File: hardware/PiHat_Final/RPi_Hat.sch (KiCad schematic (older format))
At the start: 0 parts

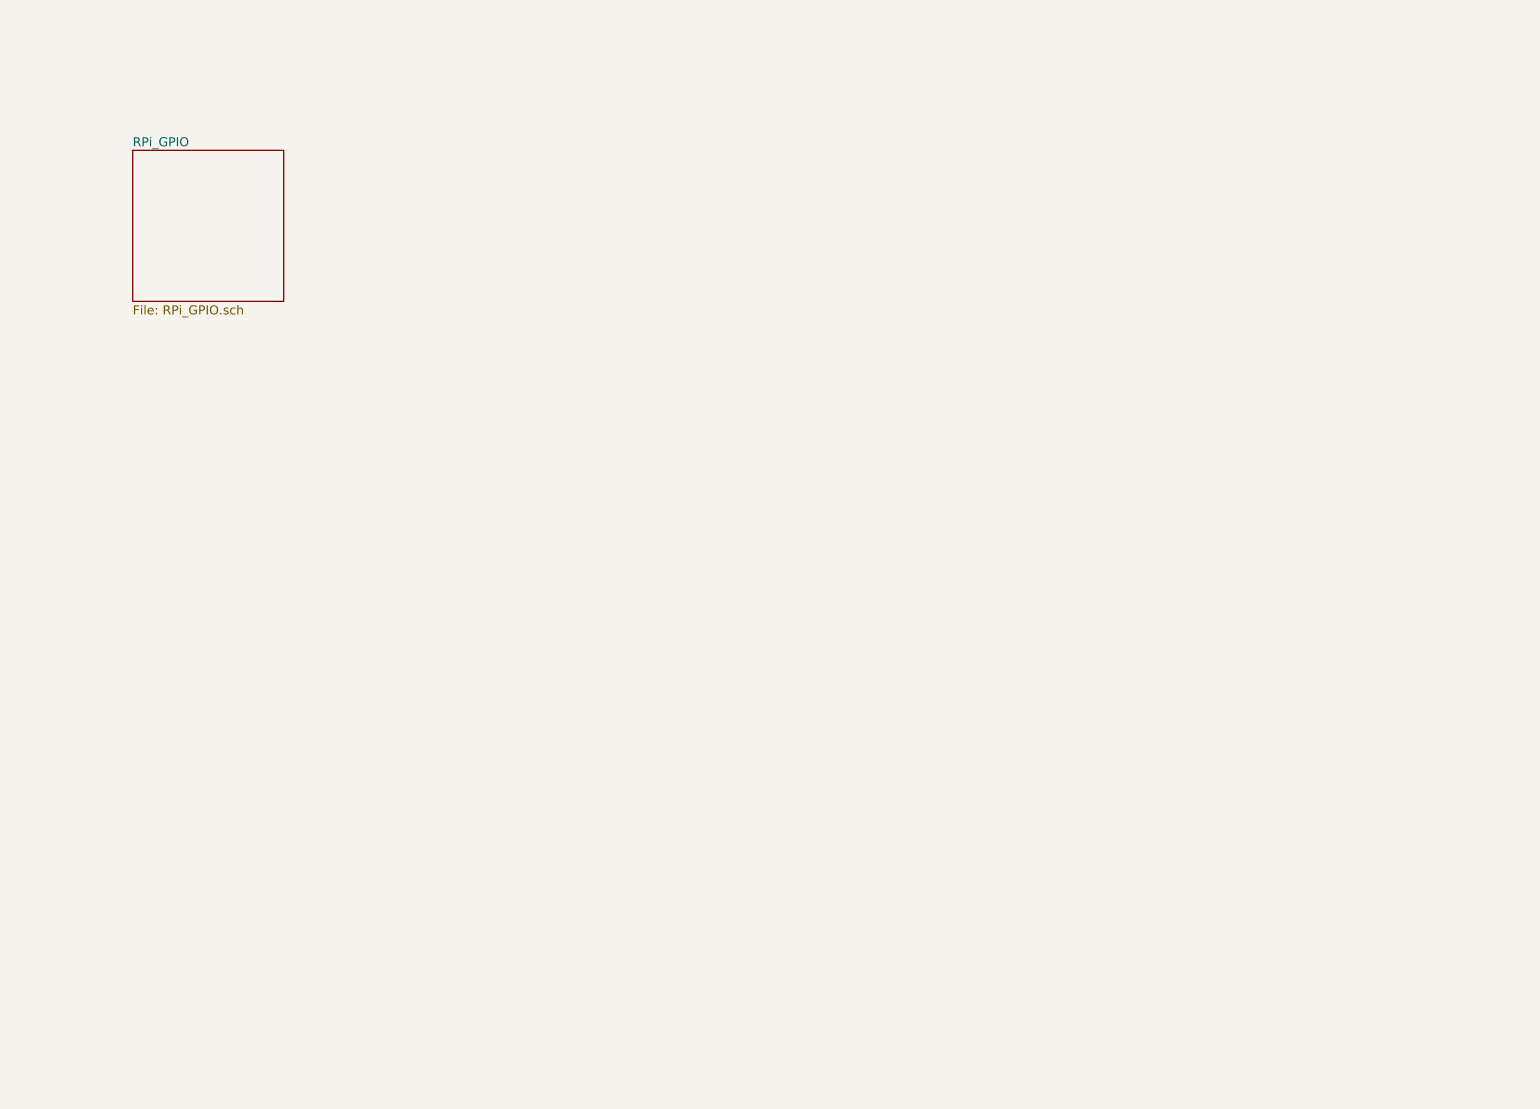
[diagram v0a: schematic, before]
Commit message: Began work on RX/TX schematic.
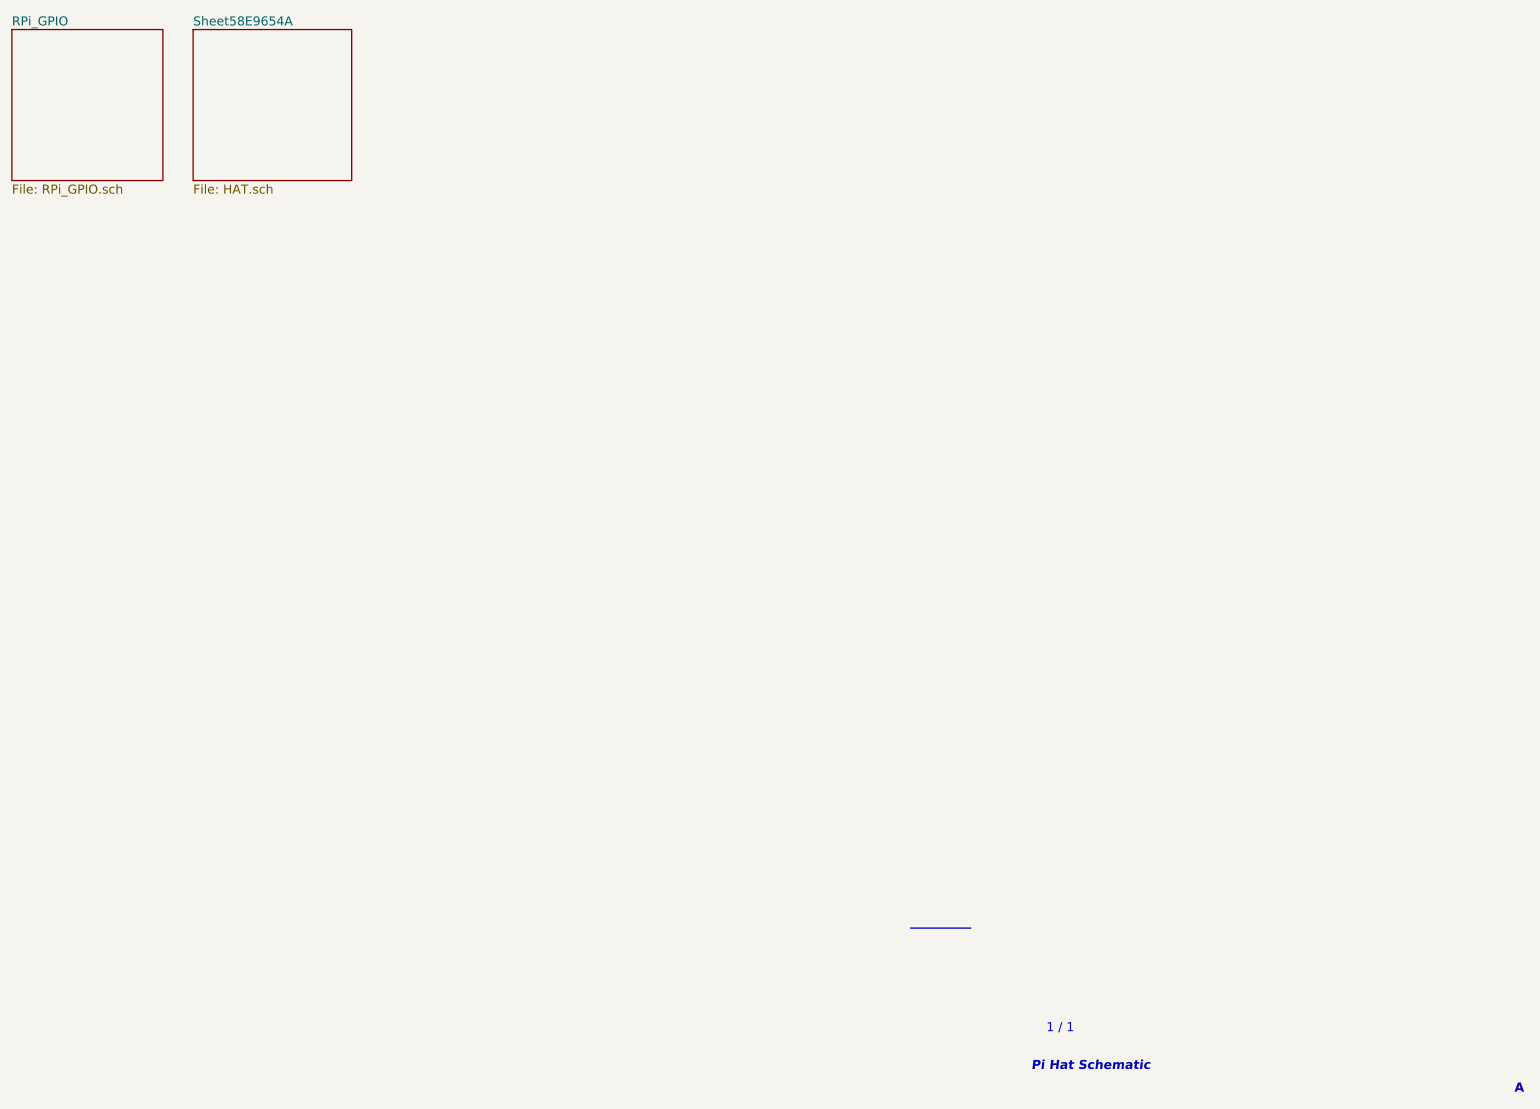
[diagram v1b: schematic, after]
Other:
- note added: "1 / 1"
- note added: "A"
- note added: "Pi Hat Schematic"
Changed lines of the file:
@@
 LIBS:contrib
 LIBS:valves
+LIBS:RFT
 LIBS:RPi_Hat-cache
 EELAYER 25 0
@@
 $Descr A4 11693 8268
 encoding utf-8
-Sheet 1 2
+Sheet 1 6
 Title ""
-Date ""
+Date "15 nov 2012"
 Rev ""
 Comp ""
@@
 $EndDescr
 $Sheet
-S 1400 1400 1000 1000
+S 600  600  1000 1000
 U 5515D395
 F0 "RPi_GPIO" 60
 F1 "RPi_GPIO.sch" 60
 $EndSheet
+$Sheet
+S 1800 600  1050 1000
+U 58E9654B
+F0 "Sheet58E9654A" 60
+F1 "HAT.sch" 60
+$EndSheet
+Wire Bus Line
+	6550 6550 6950 6550
+Text Notes 7350 7500 0    60   Italic 12
+Pi Hat Schematic
+Text Notes 7450 7250 0    60   ~ 0
+1 / 1
+Text Notes 10550 7650 0    60   ~ 12
+A
 $EndSCHEMATC
